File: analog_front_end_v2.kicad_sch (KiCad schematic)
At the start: 137 parts, among them J1 Conn_Coaxial, J3 Conn_01x01_Socket, J4 Conn_01x01_Socket, U1 ADL5531, U10 PMOD 2x6, U11 LP2985-5.0, U12 LP2985-5.0, U13 LT1363, U14 MAX 735, U15 LP2985-2.5, U16 MAX889SESA, U17 MAX6102, U18 PAT1220-C-0DB, U19 PAT1220-C-0DB, U2 ADL5531, U20 PAT1220-C-0DB, U21 PAT1220-C-0DB, U22 LP2985-3.3, U3 ADL5531, U4 PE4140B-Z, U5 ADF4360-9, U6 LTC1406, U8 LT1363, U9 PMOD 2x6

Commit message: Finished off most of the LT5546 connections, just the demod outputs & opamps to go
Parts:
- removed R11, R23, R24: 22R, Resistor_SMD:R_0603_1608Metric, symbol Device:R
- removed R13, R14: 51R, Resistor_SMD:R_0402_1005Metric, symbol Device:R
- removed R40: 50R, Resistor_SMD:R_0603_1608Metric, symbol Device:R
- removed U4: PE4140B-Z, TheEEView_Footprint_Lib:PE4140B-Z, symbol TheEEView_Global_Lib:PE4140B-Z
- added C32: 22n_25V_COG, Capacitor_SMD:C_0402_1005Metric, symbol Device:C
- added L14, L15: 72n, Inductor_SMD:L_0402_1005Metric, symbol Device:L
- added R2: 20kR, Resistor_SMD:R_0402_1005Metric, symbol Device:R
- added R5, R9: 0R, Resistor_SMD:R_0402_1005Metric, symbol Device:R
- added R6: 240R, Resistor_SMD:R_0402_1005Metric, symbol Device:R
- added R7, R8: 49R9, Resistor_SMD:R_0402_1005Metric, symbol Device:R
- added T1: JTX-4-10T_, JTX-4-10T_:JTX410T, symbol JTX-4-10T_:JTX-4-10T_
- added U23: PMOD 2x6, Connector_PinHeader_1.00mm:PinHeader_2x06_P1.00mm_Vertical, symbol TheEEView_Global_Lib:PMOD_2x6
- C28, C29: MOC CC0402JRNPO9BN101 -> (none); Tolerance 5% -> (none)
- L18: Tolerance (none) -> 30%
- R10: value 22R -> 0R; footprint Resistor_SMD:R_0603_1608Metric -> Resistor_SMD:R_0402_1005Metric; MOC RMCF0603FT22R0 -> (none); Size 0603 -> 0402; Tolerance 1% -> (none)
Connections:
- net 3.3V: now also R2.2
- net 3.3V_PMOD: now also C28.2, C29.2, U5.4 (RFOUTA), U5.5 (RFOUTB), L14.2, L15.1, U23.12, U23.6
- net DEMOD_VCTRL: now also U23.10
- net GND: now also R5.2, R7.2, R8.1, T1.3 (PRIMARY_DOT), U23.11, U23.5
- net REFOUTB: now reaches R10.2
- net LO-: now reaches R10.1
- net LO-: now also U7.10 (2xLO-), R6.1, T1.4 (SECONDARY)
- net LO+: now reaches U7.11 (2xLO+)
- net LO+: now also R6.2, R9.1, T1.6 (SECONDARY_DOT)
- net at U7.12 (STBY): now also R5.1
- net at U7.9 (EN): now also R2.1
- net PLL_OUT: now reaches C29.1
- net PLL_OUT: now also C32.2; no longer U5.5 (RFOUTB)
- new net: L14.1, R8.2
- new net: C32.1, T1.1 (PRIMARY)
- new net: L15.2, R7.1
- new net REFOUTA: R9.2
- no-connect marks 27 -> 29
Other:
- note added: "PWM Output from FPGA"
- note removed: "LO = Local Oscillator Input RF = RF Input"
- note removed: "Note: Footprint has an unconnected pin 7 exposed solder pad"
- note removed: "RF Mixer"
- note removed: "T-Pad 50ohm attenuator (change middle resistor on board if needed)"
- note removed: "TODO: Finish I/Q component creation"
- moved on the sheet: C24, C25, C26

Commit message: Start adding analog signal processing post demod I/Q signals
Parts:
- added C33: 1u_16V, Capacitor_SMD:C_0402_1005Metric, symbol Device:C
- added R11: 20kR, Resistor_SMD:R_0402_1005Metric, symbol Device:R
- added U24, U25, U26, U4: ADA4899-1YRDZ, ADA4899-1YRDZ:SOIC127P600X175-9N, symbol ADA4899-1YRDZ:ADA4899-1YRDZ
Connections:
- net REFOUTA is gone; now on net PLL_OUT: R9.2
- net DEMOD_I+: now also C33.1, R11.1
- net GND: now also R11.2
- net REFOUTB: now also C28.1
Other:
- note added: "I/Q Demod"
- note added: "TODO: Add a small LCD to display FM freq and vol bars"
- moved on the sheet: C21, C22, C23, C24, C25, C26, C27, C28, C29, C30, C31, C32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

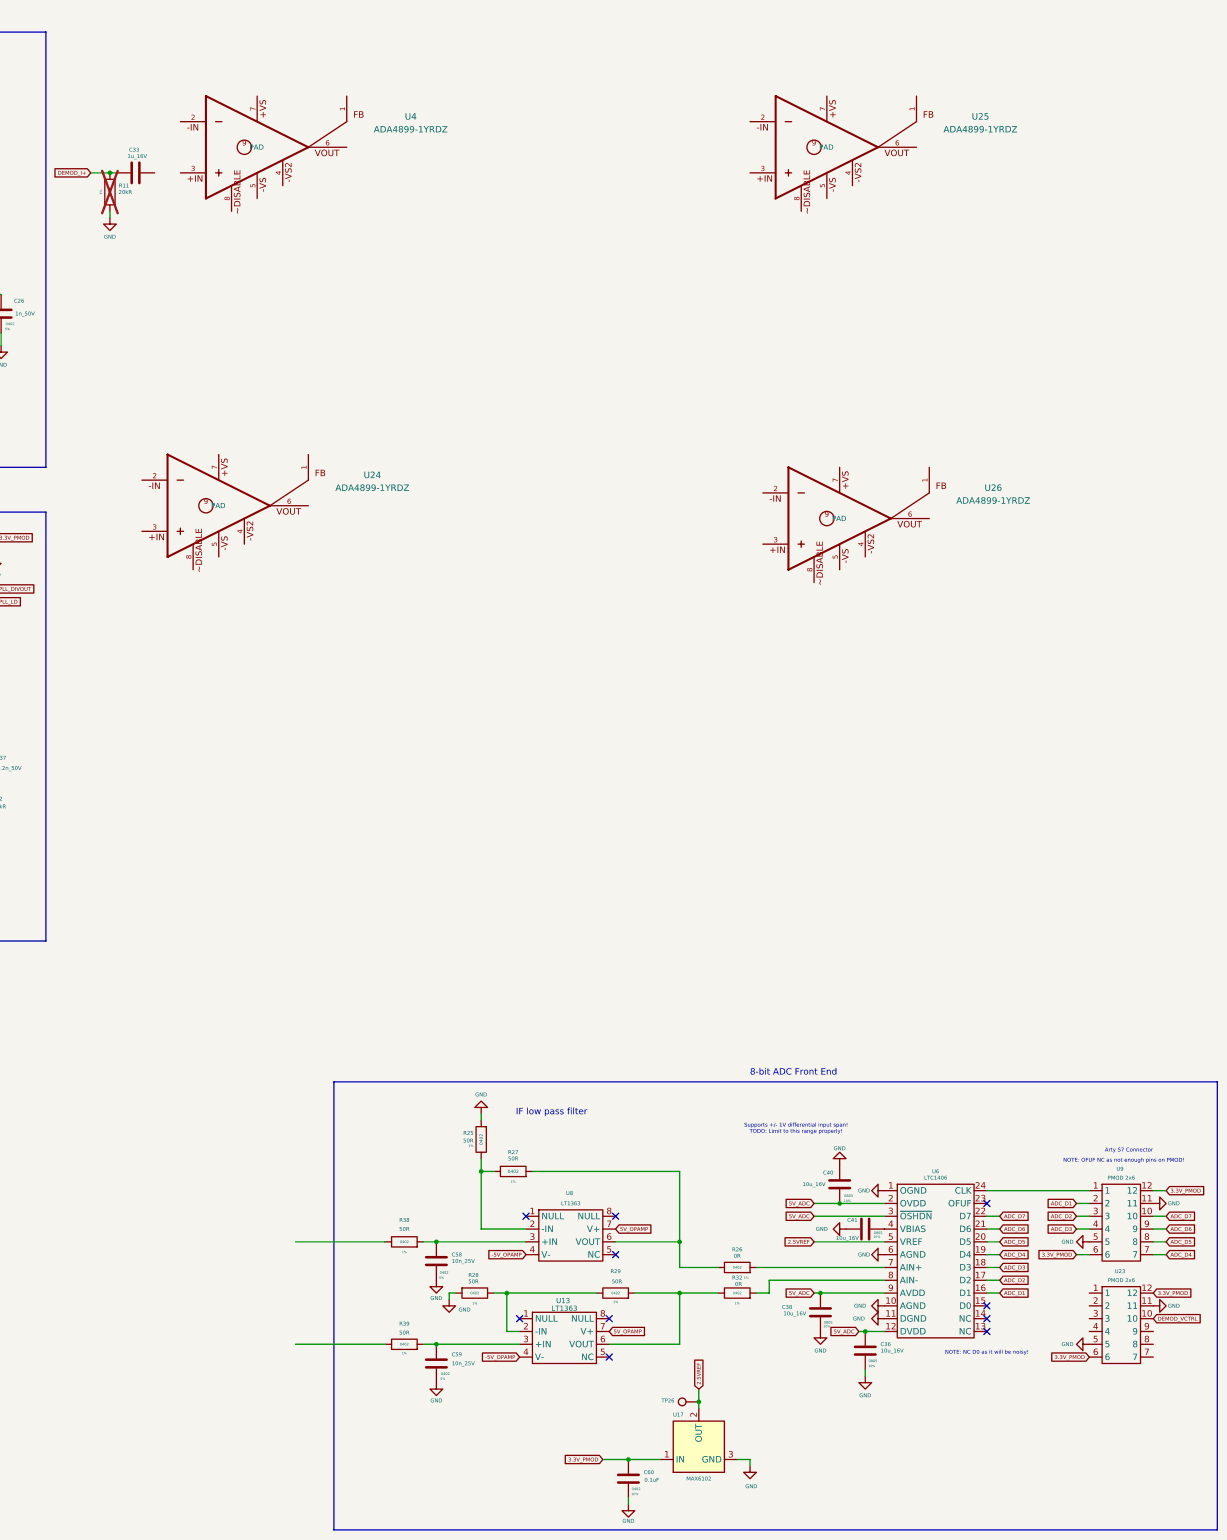
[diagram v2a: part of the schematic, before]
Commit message: Further work on IF filters/cleanup of old now redundant 8-bit ADC circuitry
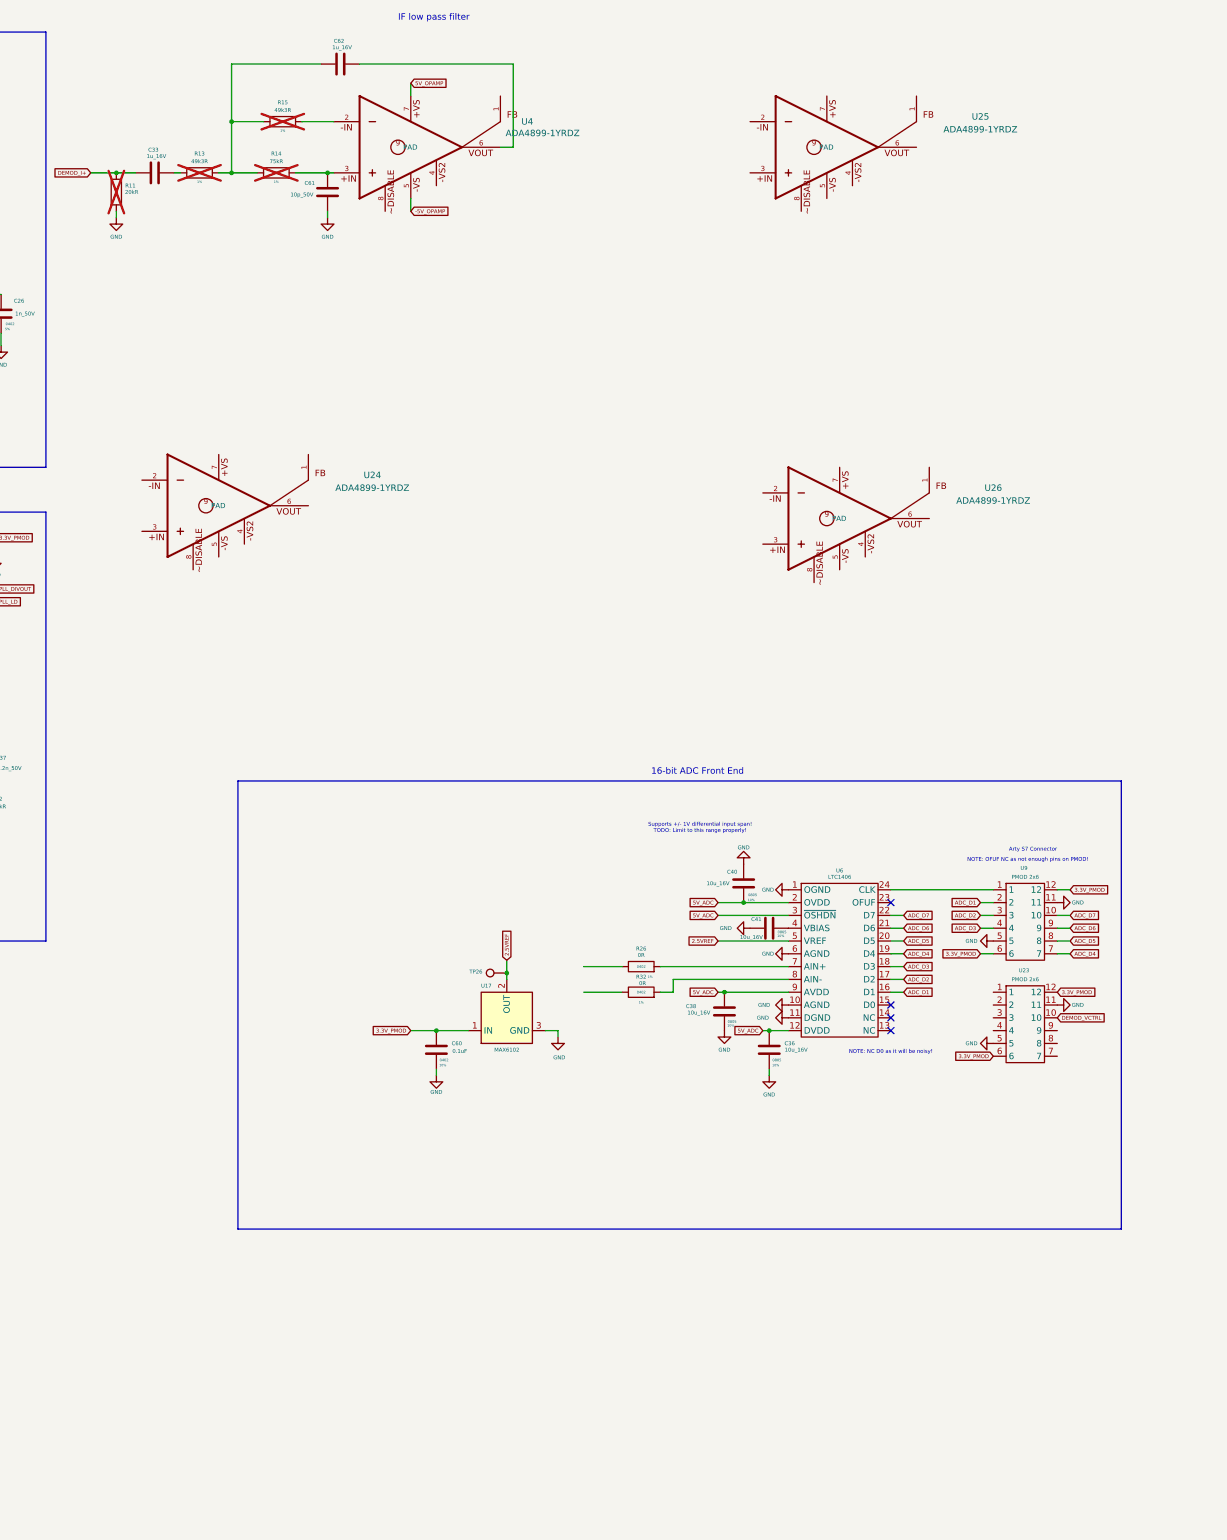
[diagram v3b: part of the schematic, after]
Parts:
- removed C58, C59: 10n_25V, Capacitor_SMD:C_0402_1005Metric, symbol Device:C
- removed R25, R27, R28, R29, R38, R39: 50R, Resistor_SMD:R_0402_1005Metric, symbol Device:R
- removed U13, U8: LT1363, Package_SO:SOIC-8_5.3x5.3mm_P1.27mm, symbol TheEEView_Global_Lib:LT1363
- added C61: 10p_50V, Capacitor_SMD:C_0402_1005Metric, symbol Device:C
- added C62: 1u_16V, Capacitor_SMD:C_0402_1005Metric, symbol Device:C
- added R13, R15: 49k3R, Resistor_SMD:R_0402_1005Metric, symbol Device:R
- added R14: 75kR, Resistor_SMD:R_0402_1005Metric, symbol Device:R
- C33: MOC GRM1555C1H102JA01D -> (none)
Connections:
- net -5V_OPAMP: now also U4.5
- net 5V_OPAMP: now also U4.7
- net GND: now also C61.2
- net at C33.2: now also R13.1
- net at U4.2: now also R15.2
- net at U4.3: now also C61.1, R14.2
- net at U4.6: now also C62.2
- new net: C62.1, R13.2, R14.1, R15.1
- no-connect marks 29 -> 23
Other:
- note added: "16-bit ADC Front End"
- note removed: "8-bit ADC Front End"
- moved on the sheet: C33, C36, C38, C40, C41, C60, R11, R26, R32, TP26, U17, U23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
